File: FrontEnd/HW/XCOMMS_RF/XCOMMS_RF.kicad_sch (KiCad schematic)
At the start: 82 parts, among them J1 SMA, J2 SMA, J3 SFC-110-T2-F-D-A-TR, U1 SIM-14+, U2 HMC788ALP2ETR, U3 HMC952ALP5GE, U4 LMX2572RHAT, U5 HMC788ALP2ETR, U6 AD8031, U7 ADT7310, Y1 TCXO 25 MHz

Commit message: XCOMMS_RF and XCOMMS_Interface KiCad design updated
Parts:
- removed C13, C29, C30, C37, C38, C39, C44, C45, C48: 100nF, Capacitor_SMD:C_0603_1608Metric, symbol Device:C
- removed C14, C43, C47, C5, C7: 1uF, Capacitor_SMD:C_0603_1608Metric, symbol Device:C
- removed C21, C6, C8, C9: 10uF, Capacitor_SMD:C_0805_2012Metric, symbol Device:C
- removed C40: 2nF, Capacitor_SMD:C_0603_1608Metric, symbol Device:C
- removed C46: 39nF, Capacitor_SMD:C_0603_1608Metric, symbol Device:C
- removed C49, C50, C51: Cap Semi, 0603 SMD Capacitor, symbol XCOMMS_RF-altium-import:1_Cap Semi
- removed J3: SFC-110-T2-F-D-A-TR, GGS_Connectors:SAMTEC_SFC-110-T2-F-D-A-TR, symbol XCOMMS_RF-altium-import:0_mirrored_SFC-110-T2-F-D-A-TR
- removed R1, R3, R4: 50 RF, Resistor_SMD:R_0402_1005Metric, symbol Device:R
- removed R10: Res3, 0603 SMD Resistor, symbol XCOMMS_RF-altium-import:3_Res3
- removed R2: 180, Resistor_SMD:R_0603_1608Metric, symbol Device:R
- removed R5, R6, R9: Res3, 0603 SMD Resistor, symbol XCOMMS_RF-altium-import:1_Res3
- removed R7, R8: Res3, 0603 SMD Resistor, symbol XCOMMS_RF-altium-import:2_Res3
- removed U4: LMX2572RHAT, SamacSys_Footprints:QFN50P600X600X100-41N-D, symbol SamacSys_Parts:LMX2572RHAT
- removed Y1: TCXO 25 MHz, ECS-TXO-2016, symbol XCOMMS_RF-altium-import:0_ECS-TXO-2016
- added C50: 100pF, Capacitor_SMD:C_0402_1005Metric, symbol Device:C
- added J3: SFC-110-T2-F-D-A-TR, GGS_Connectors:SAMTEC_SFC-110-T2-F-D-A-TR, symbol GGS_Connectors:SFC-110-T2
- added R10, R7, R8, R9: 10k, symbol Device:R
- added R5, R6: 100k, symbol Device:R
- U2, U5: symbol SamacSys_Parts:HMC788ALP2ETR -> GGS_RF:HMC788A
- U6: symbol XCOMMS_RF-altium-import:0_AD8031 -> GGS_Miscellaneous:AD8031
- U7: symbol XCOMMS_RF-altium-import:0_ADT7310 -> GGS_Miscellaneous:ADT7310
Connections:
- net 5V is gone; now on net +5V: U6.5 (+VS)
- net +3V3: now also C50.2, J3.02
- net +5V: now also J3.01, R5.2, R6.2
- net GND: now also C50.1, J3.06, J3.08, J3.10, J3.11, J3.12, J3.13, R10.1
- net LO_EN: now also J3.05
- net PLL_CSB: now also J3.14
- net SCK: now also J3.15
- net SDI: now also J3.19
- net SDO: now also J3.17
- net T_CSB: now also J3.07
- net Tx_CE: now also J3.09
- net Tx_PM: now also J3.04, R8.2
- net Vd_PA: now also J3.03
- net Vdet: now also R6.1, R7.1
- net Vg_PA1: now also J3.20
- net Vg_PA2: now also J3.18
- net Vg_PA3: now also J3.16
- net Vref: now also R5.1, R9.2
- net TP2_In: now reaches C1.2, TP2.1 (IN)
- net AMP1_Out: now reaches C1.1, L1.1, U2.5 (RFOUT)
- net Mixer_Out: now reaches FL1.1 (in), TP1.1 (IN), U1.4 (RF)
- net at U6.4 (-IN): now also R7.2, R8.1
- net at U6.3 (+IN): now also R10.2, R9.1
- net PLL_Out: now reaches U5.2 (RFIN)
- net TP1_Out: now reaches C2.1, TP1.3 (OUT)
- net AMP1_In: now reaches C2.2, U2.2 (RFIN)
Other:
- added sheet LocalOscillator (XCOMMS_RF_LocalOscillator.kicad_sch)
- note added: "Frequency Up-Conversion"
- note added: "LO Generation"
- note added: "Power Amplifier"
- note added: "Pre-Amplification"
- note added: "Temperature and Transmitted Power"
- moved on the sheet: C1, C10, C11, C12, C15, C16, C17, C18, C19, C2, C20, C22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

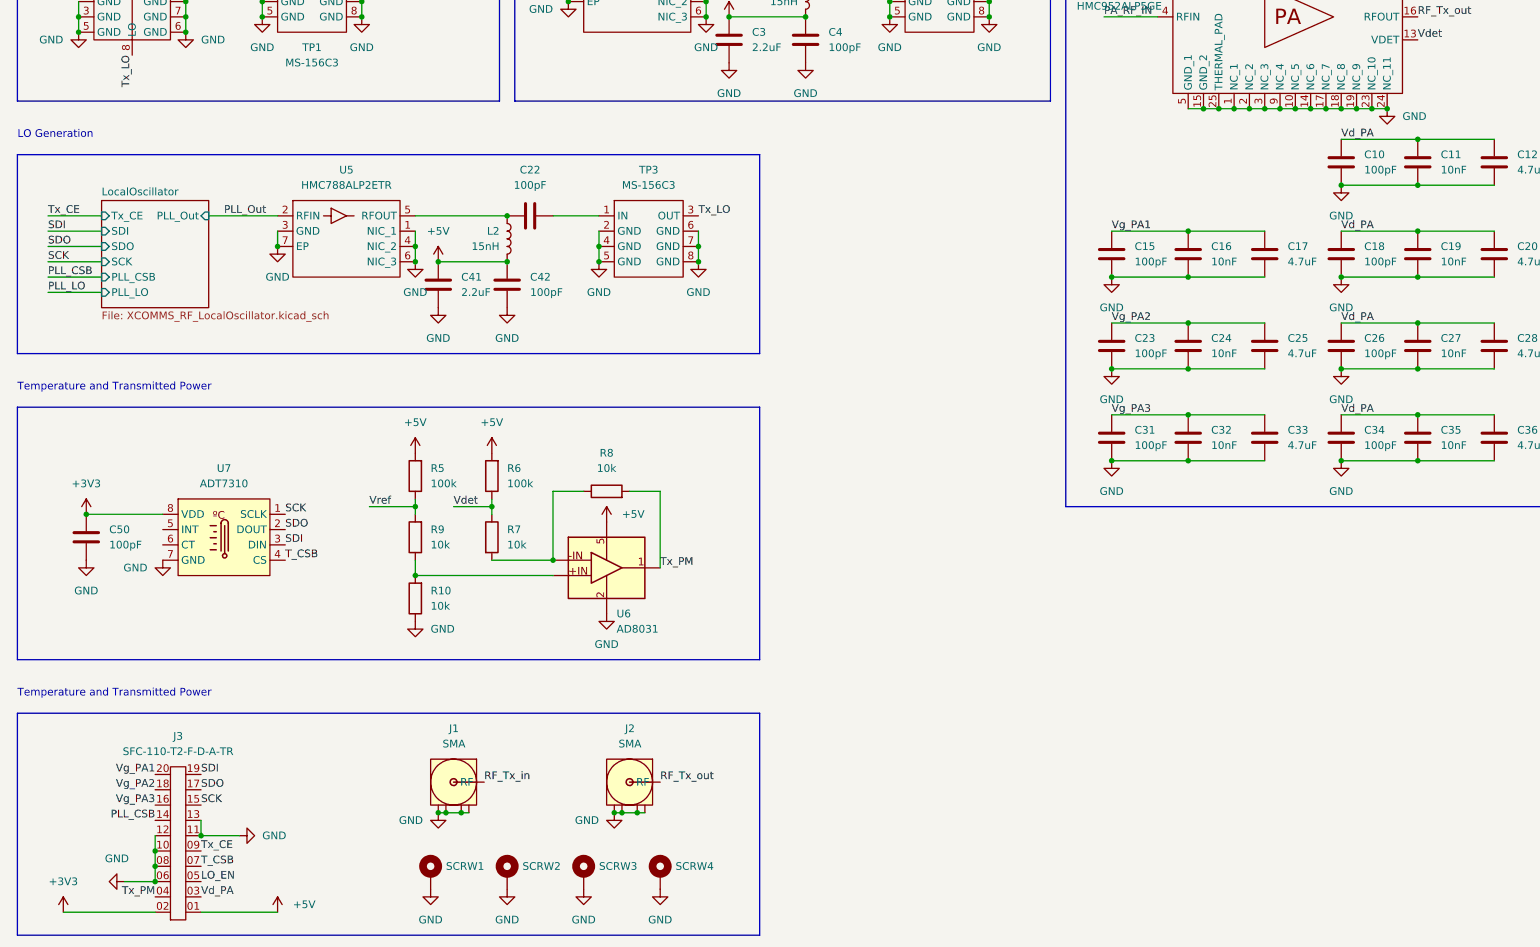
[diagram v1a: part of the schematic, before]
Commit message: XCOMMS_RF ported to KiCad
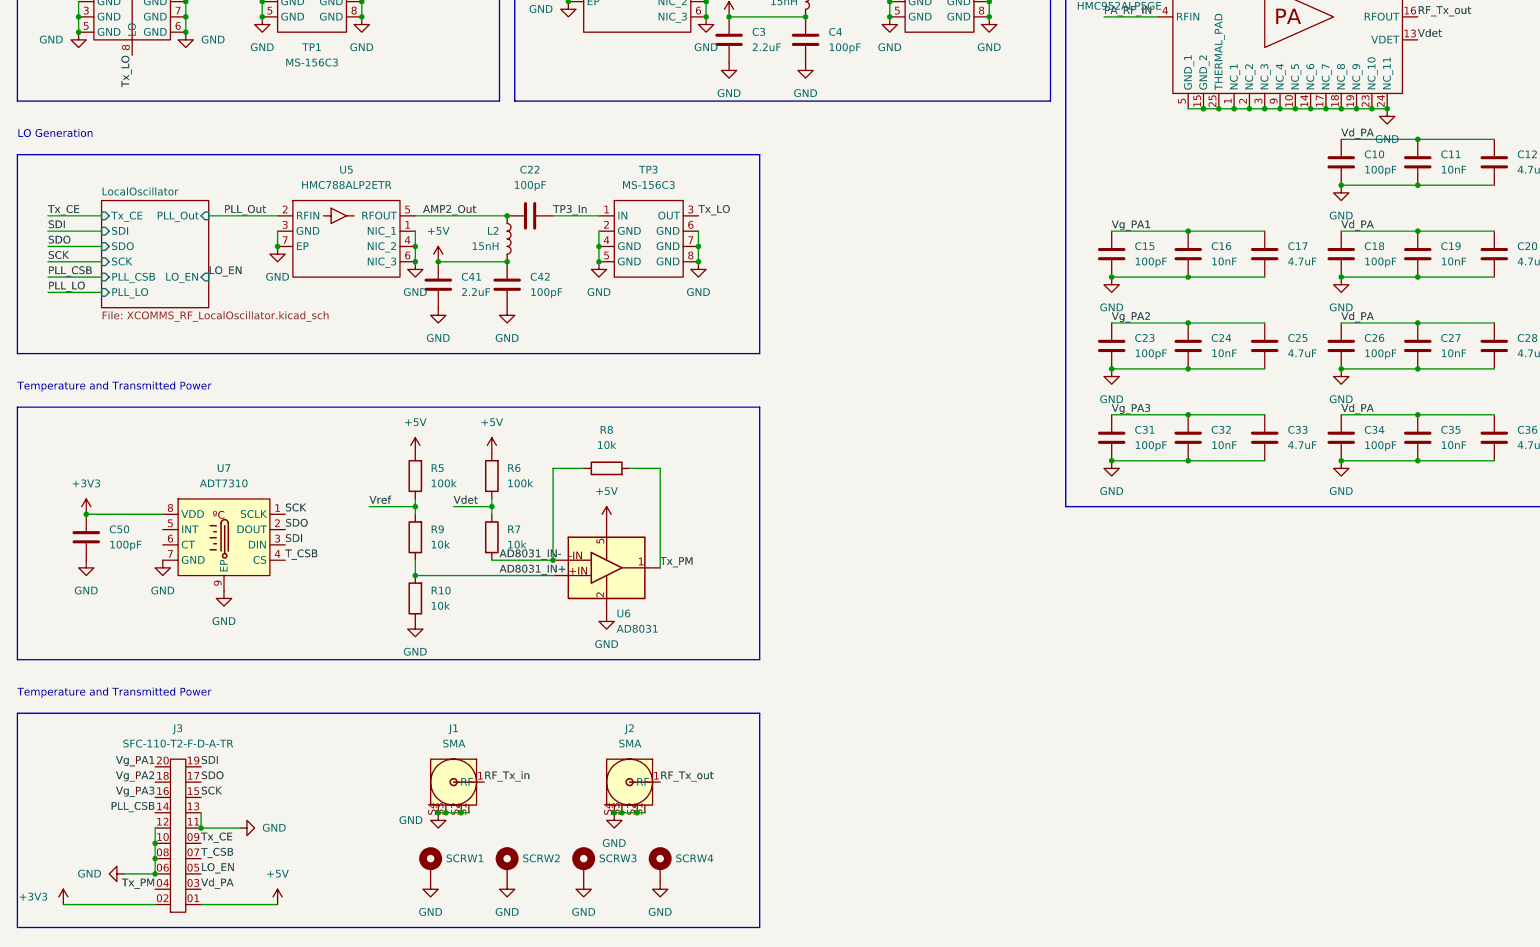
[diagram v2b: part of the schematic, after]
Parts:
- R10, R5, R6, R7, R8, R9: footprint (none) -> Resistor_SMD:R_0603_1608Metric
- U7: footprint SOIC-8 -> Package_SO:SOIC-8-1EP_3.9x4.9mm_P1.27mm_EP2.41x3.81mm
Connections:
- net GND: now also J1.S1, J1.S2, J1.S3, J1.S4, J2.S1, J2.S2, J2.S3, J2.S4, U7.9 (EP); no longer J1.2, J1.3, J1.4, J1.5, J2.2, J2.3, J2.4, J2.5
- net TP3_In: now reaches C22.2, TP3.1 (IN)
- net AMP2_Out: now reaches C22.1, L2.1, U5.5 (RFOUT)
- net AD8031_IN-: now reaches R7.2, R8.1, U6.4 (-IN)
- net AD8031_IN+: now reaches R10.2, R9.1, U6.3 (+IN)
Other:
- sheet LocalOscillator ports: added LO_EN; removed none
- moved on the sheet: J3, R8, SCRW1, SCRW2, SCRW3, SCRW4

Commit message: XCOMS_RF updated
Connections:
- net Tx_CE renamed PLL_CE
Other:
- sheet LocalOscillator ports: added PLL_CE; removed Tx_CE
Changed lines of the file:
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@@
     (effects (font (size 1.27 1.27)) (justify left bottom))
   )
-  (label "Tx_CE" (at 53.34 180.34 0)
+  (label "PLL_CE" (at 53.34 180.34 0)
     (effects (font (size 1.27 1.27)) (justify left bottom))
   )
@@
     (effects (font (size 1.27 1.27)) (justify left bottom))
   )
-  (label "Tx_CE" (at 27.94 76.2 0)
+  (label "PLL_CE" (at 27.94 76.2 0)
     (effects (font (size 1.27 1.27)) (justify left bottom))
   )
@@
       (effects (font (size 1.27 1.27)) (justify left))
     )
-    (pin "Tx_CE" input (at 36.83 76.2 180)
+    (pin "PLL_CE" input (at 36.83 76.2 180)
       (effects (font (size 1.27 1.27)) (justify left))
     )
@@
     )
     (path "/14b0b94e-1900-4eef-997c-90e0c19fc280/22c7397a-07ae-4561-971a-8b7e626239ce"
-      (reference "C7") (unit 1) (value "1uF") (footprint "Capacitor_SMD:C_0603_1608Metric")
+      (reference "C7") (unit 1) (value "10nF") (footprint "Capacitor_SMD:C_0603_1608Metric")
     )
     (path "/14b0b94e-1900-4eef-997c-90e0c19fc280/9676cde1-11fc-48d4-bc56-63775b1b64db"
@@
     )
     (path "/14b0b94e-1900-4eef-997c-90e0c19fc280/1f5b78c8-1d71-4c92-bcfa-5ec7a636163a"
-      (reference "C21") (unit 1) (value "10uF") (footprint "Capacitor_SMD:C_0805_2012Metric")
+      (reference "C21") (unit 1) (value "470nF") (footprint "Capacitor_SMD:C_0805_2012Metric")
     )
     (path "/9e916e8d-ae47-4a69-aa9a-bf1f392290ef"

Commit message: XCOMMS_RF update
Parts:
- removed FL1: NotchFilter, Notch_5600to6100MHz, symbol XCOMMS_RF-altium-import:1_NotchFilter
- added FL1: HFCW-7000+, GGS_RF:JC0603C, symbol GGS_RF:HFCW-7000+
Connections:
- net GND: now also FL1.2 (GND), FL1.4 (GND), FL1.5 (GND), FL1.6 (GND)
- net Mixer_Out: now also FL1.1 (In); no longer TP1.1 (IN)
- net RF_Tx_in renamed RF_in
- net RF_Tx_out renamed RF_out
- new net FL_Out: FL1.3 (Out), TP1.1 (IN)
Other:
- note added: "Connectors and Screws"
- moved on the sheet: C1, C10, C11, C12, C15, C16, C17, C18, C19, C2, C20, C22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

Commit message: PA TB
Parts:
- SCRW1: footprint MountingHole:MountingHole_3.2mm_M3_Pad_Via -> MountingHole:MountingHole_2.7mm_M2.5_Pad_Via
- SCRW2, SCRW3, SCRW4: footprint MountingHole:MountingHole_3.2mm_M3_Pad_Via -> MountingHole:MountingHole_2.7mm_Pad_Via
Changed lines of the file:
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@@
   (symbol (lib_id "power:GND") (at 21.59 45.72 0) (unit 1)
     (in_bom yes) (on_board yes) (fields_autoplaced)
-    (property "Reference" "#PWR?" (id 0) (at 21.59 52.07 0)
+    (property "Reference" "#PWR0109" (id 0) (at 21.59 52.07 0)
       (effects (font (size 1.27 1.27)) hide)
     )
@@
       (effects (font (size 1.27 1.27)) hide)
     )
-    (property "Footprint" "MountingHole:MountingHole_3.2mm_M3_Pad_Via" (id 2) (at 121.92 184.15 0)
+    (property "Footprint" "MountingHole:MountingHole_2.7mm_Pad_Via" (id 2) (at 121.92 184.15 0)
       (effects (font (size 1.27 1.27)) hide)
     )
@@
   (symbol (lib_id "power:GND") (at 64.77 41.91 0) (unit 1)
     (in_bom yes) (on_board yes) (fields_autoplaced)
-    (property "Reference" "#PWR?" (id 0) (at 64.77 48.26 0)
+    (property "Reference" "#PWR0175" (id 0) (at 64.77 48.26 0)
       (effects (font (size 1.27 1.27)) hide)
     )
@@
       (effects (font (size 1.27 1.27)) (justify left) hide)
     )
-    (property "Footprint" "MountingHole:MountingHole_3.2mm_M3_Pad_Via" (id 2) (at 109.22 184.15 0)
+    (property "Footprint" "MountingHole:MountingHole_2.7mm_Pad_Via" (id 2) (at 109.22 184.15 0)
       (effects (font (size 1.27 1.27)) hide)
     )
@@
       (effects (font (size 1.27 1.27)) hide)
     )
-    (property "Footprint" "MountingHole:MountingHole_3.2mm_M3_Pad_Via" (id 2) (at 96.52 184.15 0)
+    (property "Footprint" "MountingHole:MountingHole_2.7mm_Pad_Via" (id 2) (at 96.52 184.15 0)
       (effects (font (size 1.27 1.27)) hide)
     )
@@
       (effects (font (size 1.27 1.27)) (justify left) hide)
     )
-    (property "Footprint" "MountingHole:MountingHole_3.2mm_M3_Pad_Via" (id 2) (at 83.82 184.15 0)
+    (property "Footprint" "MountingHole:MountingHole_2.7mm_M2.5_Pad_Via" (id 2) (at 83.82 184.15 0)
       (effects (font (size 1.27 1.27)) hide)
     )
@@
   (symbol (lib_id "power:GND") (at 48.26 41.91 0) (unit 1)
     (in_bom yes) (on_board yes) (fields_autoplaced)
-    (property "Reference" "#PWR?" (id 0) (at 48.26 48.26 0)
+    (property "Reference" "#PWR0174" (id 0) (at 48.26 48.26 0)
       (effects (font (size 1.27 1.27)) hide)
     )
@@
   (symbol (lib_id "power:GND") (at 39.37 45.72 0) (unit 1)
     (in_bom yes) (on_board yes) (fields_autoplaced)
-    (property "Reference" "#PWR?" (id 0) (at 39.37 52.07 0)
+    (property "Reference" "#PWR0112" (id 0) (at 39.37 52.07 0)
       (effects (font (size 1.27 1.27)) hide)
     )
@@
       (reference "#PWR0108") (unit 1) (value "+5V") (footprint "")
     )
+    (path "/07bafb91-99e2-4082-8b6e-8175bdd2c01b"
+      (reference "#PWR0109") (unit 1) (value "GND") (footprint "")
+    )
     (path "/4040a07f-25cf-447d-98d2-351b395831b3"
       (reference "#PWR0110") (unit 1) (value "GND") (footprint "")
@@
       (reference "#PWR0111") (unit 1) (value "GND") (footprint "")
     )
+    (path "/a6692cd4-96b3-443d-8be6-accd4301b028"
+      (reference "#PWR0112") (unit 1) (value "GND") (footprint "")
+    )
     (path "/3bb43694-2f07-402c-9bac-c54bf6410d8e"
       (reference "#PWR0113") (unit 1) (value "GND") (footprint "")
@@
       (reference "#PWR0173") (unit 1) (value "GND") (footprint "")
     )
+    (path "/55f92a59-8c39-45cc-91eb-7b2e753eba53"
+      (reference "#PWR0174") (unit 1) (value "GND") (footprint "")
+    )
+    (path "/17fccb23-1284-49b1-b8e0-e599e0db79ac"
+      (reference "#PWR0175") (unit 1) (value "GND") (footprint "")
+    )
     (path "/6313534e-7526-48a8-a898-3b99488869c2"
       (reference "#PWR0177") (unit 1) (value "GND") (footprint "")
@@
       (reference "#PWR0187") (unit 1) (value "+5V") (footprint "")
     )
-    (path "/07bafb91-99e2-4082-8b6e-8175bdd2c01b"
-      (reference "#PWR?") (unit 1) (value "GND") (footprint "")
-    )
-    (path "/17fccb23-1284-49b1-b8e0-e599e0db79ac"
-      (reference "#PWR?") (unit 1) (value "GND") (footprint "")
-    )
-    (path "/55f92a59-8c39-45cc-91eb-7b2e753eba53"
-      (reference "#PWR?") (unit 1) (value "GND") (footprint "")
-    )
-    (path "/a6692cd4-96b3-443d-8be6-accd4301b028"
-      (reference "#PWR?") (unit 1) (value "GND") (footprint "")
-    )
     (path "/d3ecef9c-fb94-4e9d-927d-bb7dc8fea0fd"
       (reference "C1") (unit 1) (value "100pF") (footprint "Capacitor_SMD:C_0402_1005Metric")
@@
     )
     (path "/49ea3d04-dd55-4ffb-af0f-4dbf09c54d88"
-      (reference "SCRW1") (unit 1) (value "MountingHole_Pad") (footprint "MountingHole:MountingHole_3.2mm_M3_Pad_Via")
+      (reference "SCRW1") (unit 1) (value "MountingHole_Pad") (footprint "MountingHole:MountingHole_2.7mm_M2.5_Pad_Via")
     )
     (path "/2e497b62-365a-49a8-8171-e5b9c1dc77d6"
-      (reference "SCRW2") (unit 1) (value "MountingHole_Pad") (footprint "MountingHole:MountingHole_3.2mm_M3_Pad_Via")
+      (reference "SCRW2") (unit 1) (value "MountingHole_Pad") (footprint "MountingHole:MountingHole_2.7mm_Pad_Via")
     )
     (path "/227398ff-7060-4354-a52f-5d194ba6472b"
-      (reference "SCRW3") (unit 1) (value "MountingHole_Pad") (footprint "MountingHole:MountingHole_3.2mm_M3_Pad_Via")
+      (reference "SCRW3") (unit 1) (value "MountingHole_Pad") (footprint "MountingHole:MountingHole_2.7mm_Pad_Via")
     )
     (path "/0c48b150-3145-4990-a667-72f5d61838fc"
-      (reference "SCRW4") (unit 1) (value "MountingHole_Pad") (footprint "MountingHole:MountingHole_3.2mm_M3_Pad_Via")
+      (reference "SCRW4") (unit 1) (value "MountingHole_Pad") (footprint "MountingHole:MountingHole_2.7mm_Pad_Via")
     )
     (path "/d4ec1feb-fe93-44fc-98b1-414acb3250de"

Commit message: XCOMMS RF update and PA EvalBoard
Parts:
- removed J1, J2: SMA, GGS_Connectors:LINX_CONSMA020.062-G, symbol GGS_Connectors:SMA
- added J1, J2: SMP-MSLD-PCE-5T, GGS_Connectors:SMP-MSLD-PCE-5T, symbol GGS_Connectors:SMP-MSLD-PCE-5T
- SCRW1: footprint MountingHole:MountingHole_2.7mm_M2.5_Pad_Via -> MountingHole:MountingHole_2.7mm_M2.5_ISO14580_Pad
- SCRW2, SCRW3, SCRW4: footprint MountingHole:MountingHole_2.7mm_Pad_Via -> MountingHole:MountingHole_2.7mm_M2.5_ISO14580_Pad
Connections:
- net GND: now also J1.2, J2.2
- net RF_in: now also J2.1
- net RF_out: now also J1.1
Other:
- note added: "19-03-2022"
- note added: "IC | V (V) | I (mA) | Power (mW) - - - - - - - - - - - - - - - - - - - PA | 6 | 1400 | 8400 -> 2000 (class C) AMP1 | 5 | 76 | 380 AMP2 | 5 | 76 | 380 AMPLO | 5 | | - - - - - - - - - - - - - - - - - - - Total |"
- note added: "Power Consumption Information"
- note added: "To do: Amp 2.4 GHz Gruix Rogers R 0 Ohm"
- note added: "XCOMMS_RF_v2"
- moved on the sheet: SCRW1, SCRW2, SCRW3, SCRW4

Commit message: XCOMMS RF update
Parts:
- added C?: 2.2uF, Capacitor_SMD:C_0603_1608Metric, symbol Device:C
- added C? (x2): 100pF, Capacitor_SMD:C_0402_1005Metric, symbol Device:C
- added L?: 15nH, Inductor_SMD:L_0603_1608Metric, symbol Device:L
- added TP?: MS-156C3, GGS_Connectors:MS-156C3, symbol GGS_Connectors:MS-156C3
- added U?: HMC788ALP2ETR, SamacSys_Footprints:SON65P200X200X90-7N-D, symbol GGS_RF:HMC788A
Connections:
- net +5V: now also C?.2, C?.2, L?.2
- net AMP1_In: now also U?.2 (RFIN)
- net AMP1_Out: now also C?.1, L?.1, U?.5 (RFOUT)
- net GND: now also C?.1, C?.1, TP?.2 (GND), TP?.4 (GND), TP?.5 (GND), TP?.6 (GND), TP?.7 (GND), TP?.8 (GND), U?.1 (NIC_1), U?.3 (GND), U?.4 (NIC_2), U?.6 (NIC_3), U?.7 (EP)
- net PA_RF_IN: now also TP?.3 (OUT)
- net TP2_In: now also C?.2, TP?.1 (IN)
- net Tx_LO: no longer TP3.3 (OUT)
- net Mixer_Out renamed Mix_Out
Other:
- note added: "Alternative 1"
- note added: "Alternative 2"
- note added: "IC | V (V) | I (mA) | Power (mW) - - - - - - - - - - - - - - - - - - - PA | 6 | 1400 | ~2500 (class C) AMP1 | 5 | 56 | 280 HMC311LP3 AMP2 | 5 | 43 | 21 HMC3587LP3BE VCO | 2.75 | 80 | 220 - - - - - - - - - - - - - - - - - - - Total | 3.2 W Notes: SDR output @ 2 GHz"
- note added: "IC | V (V) | I (mA) | Power (mW) - - - - - - - - - - - - - - - - - - - PA | 6 | 1400 | ~2500 (class C) AMP1 | 5 | 76 | 380 AMP2 | 5 | 56 | 280 HMC311LP3 AMPLO | 5 | 56 | 280 HMC311LP3 PLL | 3.3 | 90 | 300 - - - - - - - - - - - - - - - - - - - Total | 3.8 W"
- note added: "IC | V (V) | I (mA) | Power (mW) - - - - - - - - - - - - - - - - - - - PA | 6 | 1400 | ~2500 (class C) AMP1 | 5 | 76 | 380 AMP2 | 5 | 76 | 380 AMPLO | 5 | 76 | 380 PLL | 3.3 | 90 | 300 - - - - - - - - - - - - - - - - - - - Total | 4 W"
- note added: "Pre-Amplification 1"
- note added: "Pre-Amplification 2"
- note removed: "IC | V (V) | I (mA) | Power (mW) - - - - - - - - - - - - - - - - - - - PA | 6 | 1400 | 8400 -> 2000 (class C) AMP1 | 5 | 76 | 380 AMP2 | 5 | 76 | 380 AMPLO | 5 | | - - - - - - - - - - - - - - - - - - - Total |"
- note removed: "Pre-Amplification"
- moved on the sheet: C1, C10, C11, C12, C15, C16, C17, C18, C19, C2, C20, C22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
